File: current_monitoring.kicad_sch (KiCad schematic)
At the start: 24 parts, among them IC3 INA180A1QDBVRQ1, J1 DBG, Q3 PBSS4330X,135, U3 LP5912-3.3DRV, U5 74LS47, U6 ATTINY824-XUR

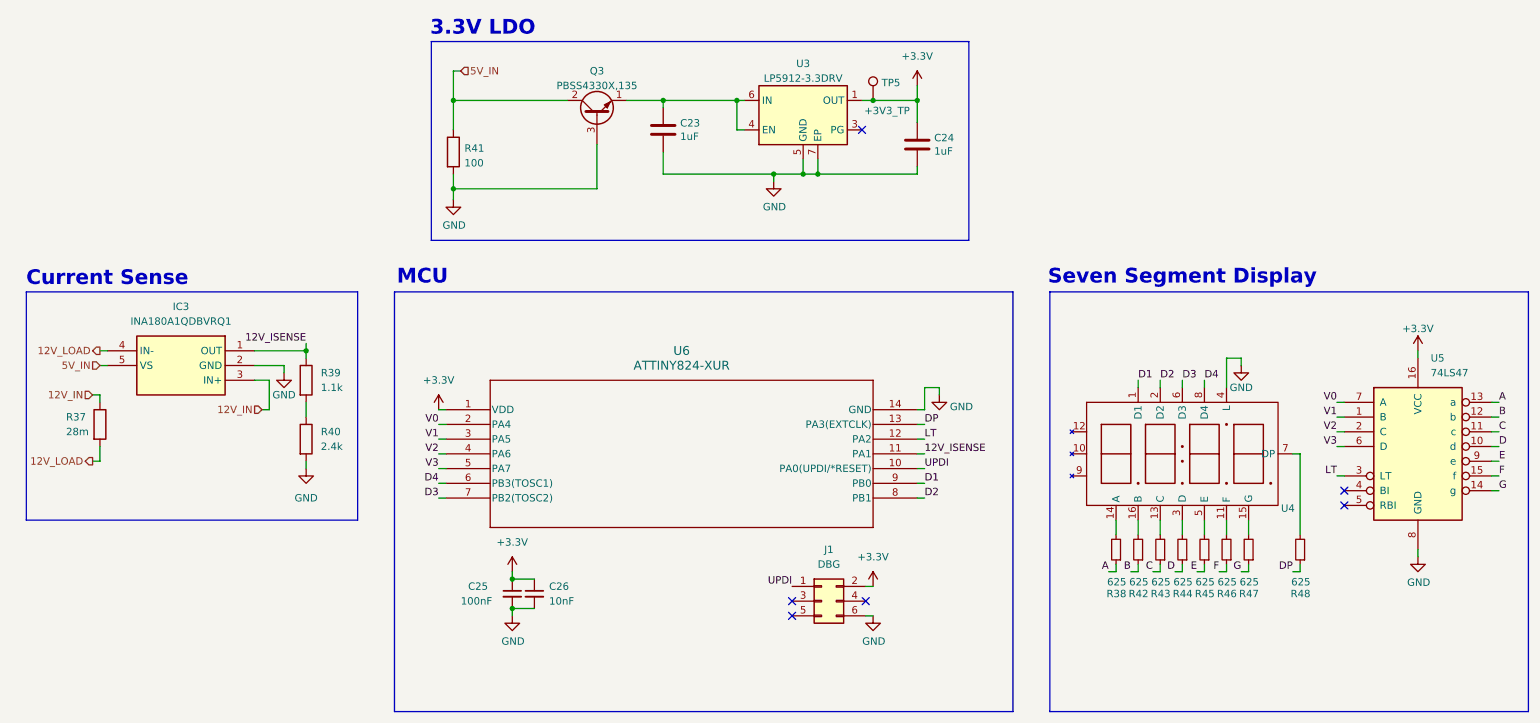
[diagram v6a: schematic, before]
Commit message: updated with some new footprints (have yet to finish footprint assignment; also need to switch out inductor for 5V buck)
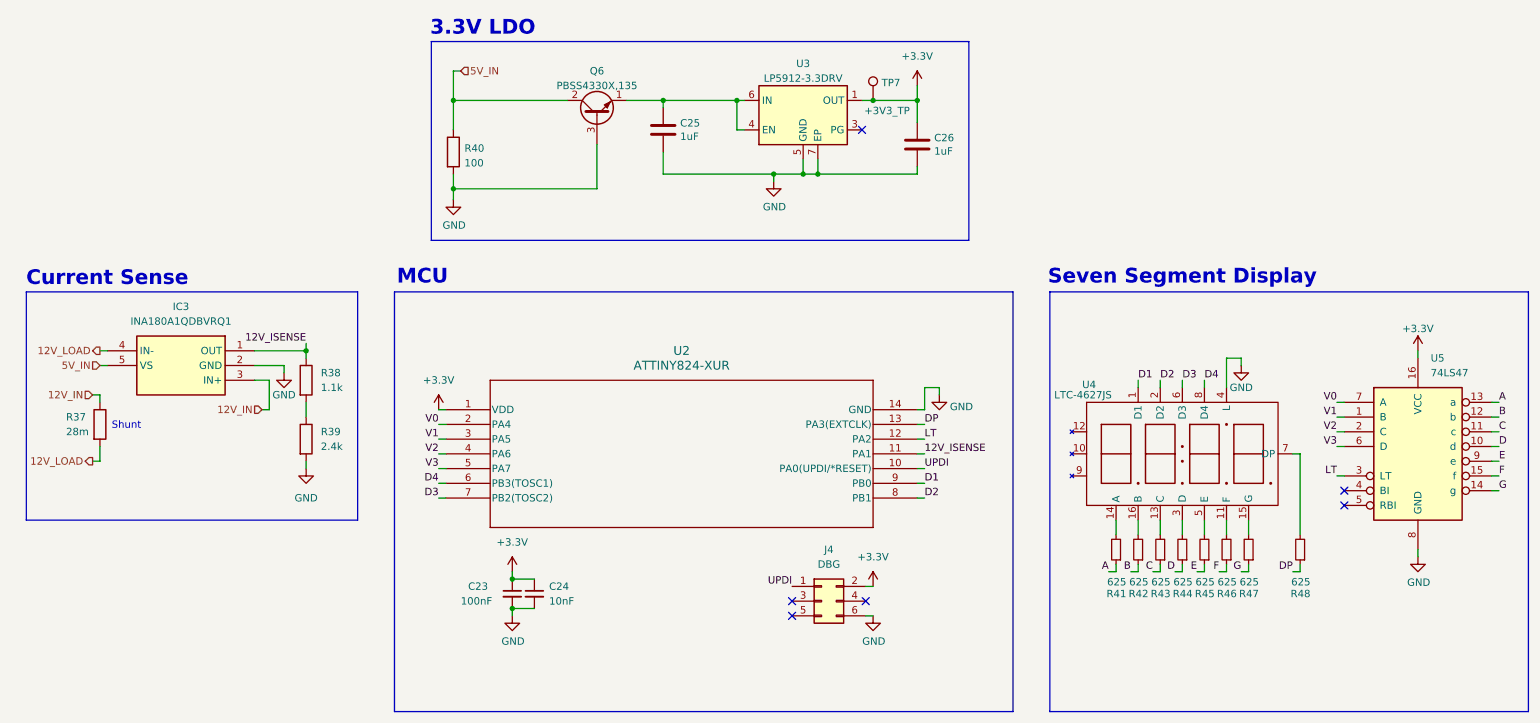
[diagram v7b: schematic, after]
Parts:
- C23: renamed from C25; footprint (none) -> Capacitor_SMD:C_0805_2012Metric
- C24: renamed from C26; footprint (none) -> Capacitor_SMD:C_0805_2012Metric
- IC3: footprint SOT95P280X145-5N -> UTSVT_ICs:SOT95P280X145-5N
- R37: Mouser Part Number (none) -> PE2512FKE7W0R028L
- R38: renamed from R39; footprint (none) -> Resistor_SMD:R_0805_2012Metric
- R39: renamed from R40; footprint (none) -> Resistor_SMD:R_0805_2012Metric
- R41: renamed from R38; footprint (none) -> Resistor_SMD:R_0805_2012Metric
- R42, R43, R44, R45, R46, R47, R48: footprint (none) -> Resistor_SMD:R_0805_2012Metric
- TP7: renamed from TP5; footprint Connector_PinHeader_2.54mm:PinHeader_1x01_P2.54mm_Vertical -> TestPoint:TestPoint_Pad_D2.5mm
- U2: renamed from U6; footprint TSSOP14_ST_MCH -> Package_SO:TSSOP-14-1EP_4.4x5mm_P0.65mm
- U4: value ~ -> LTC-4627JS; footprint (none) -> Package_DIP:DIP-14_W10.16mm_LongPads
- renumbered C23 to C25, C24 to C26, J1 to J4, Q3 to Q6, R41 to R40
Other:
- note added: "Shunt"

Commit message: changed 5v buck to TPS56A37
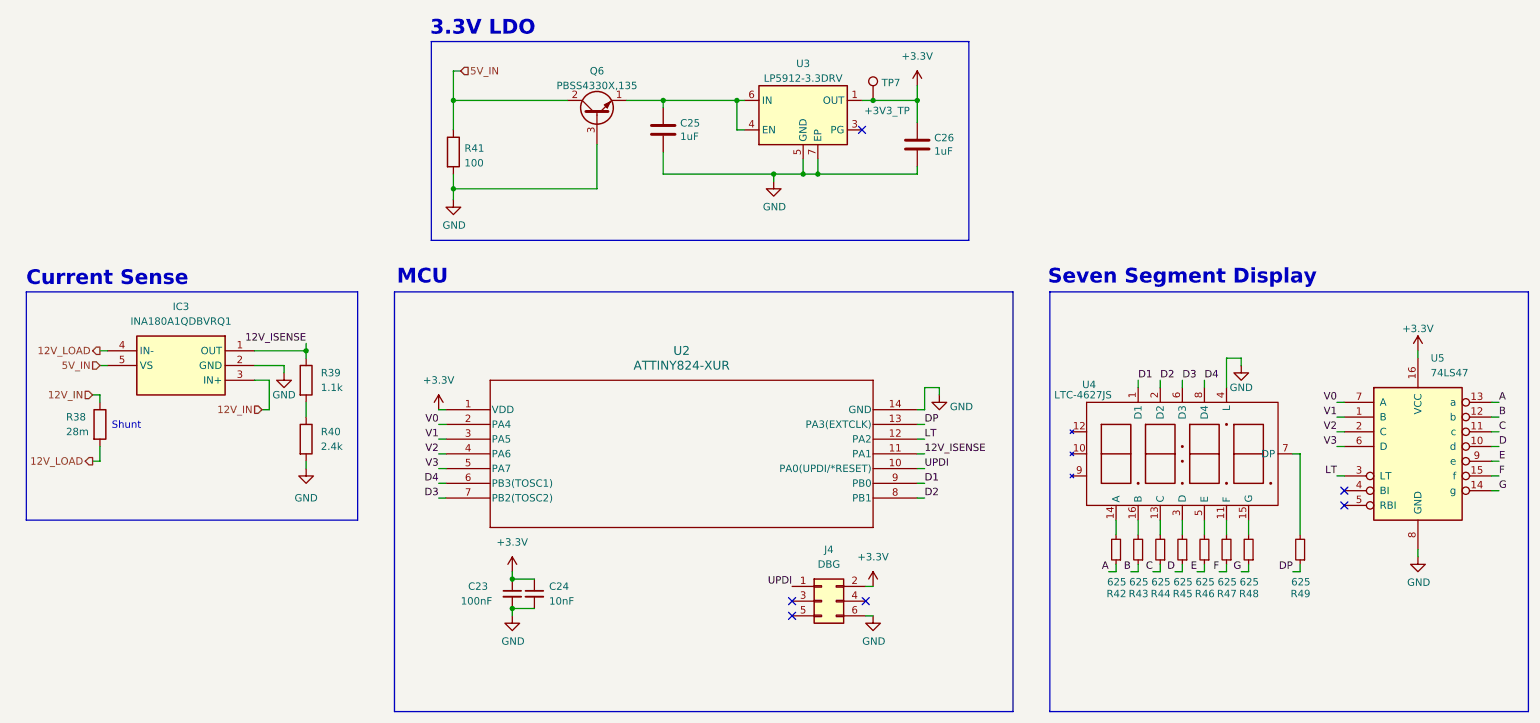
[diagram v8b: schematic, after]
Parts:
- renumbered R37 to R38, R38 to R39, R39 to R40, R40 to R41, R41 to R42, R42 to R43, R43 to R44, R44 to R45, R45 to R46, R46 to R47, R47 to R48, R48 to R49
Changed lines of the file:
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@@
 		(on_board yes)
 		(dnp no)
-		(property "Reference" "R43"
+		(property "Reference" "R44"
 			(at 217.678 121.92 0)
 			(effects
@@
 			(project "USBCPowerPCB"
 				(path "/f58400c5-df4b-4929-8d2b-33c0fe23fcd9/0ba7757f-854f-4573-bb78-e140dbbd3450"
-					(reference "R43")
+					(reference "R44")
 					(unit 1)
 				)
@@
 		(on_board yes)
 		(dnp no)
-		(property "Reference" "R42"
+		(property "Reference" "R43"
 			(at 213.868 121.92 0)
 			(effects
@@
 			(project "USBCPowerPCB"
 				(path "/f58400c5-df4b-4929-8d2b-33c0fe23fcd9/0ba7757f-854f-4573-bb78-e140dbbd3450"
-					(reference "R42")
+					(reference "R43")
 					(unit 1)
 				)
@@
 		(on_board yes)
 		(dnp no)
-		(property "Reference" "R46"
+		(property "Reference" "R47"
 			(at 229.108 121.92 0)
 			(effects
@@
 			(project "USBCPowerPCB"
 				(path "/f58400c5-df4b-4929-8d2b-33c0fe23fcd9/0ba7757f-854f-4573-bb78-e140dbbd3450"
-					(reference "R46")
+					(reference "R47")
 					(unit 1)
 				)
@@
 		(on_board yes)
 		(dnp no)
-		(property "Reference" "R44"
+		(property "Reference" "R45"
 			(at 221.488 121.92 0)
 			(effects
@@
 			(project "USBCPowerPCB"
 				(path "/f58400c5-df4b-4929-8d2b-33c0fe23fcd9/0ba7757f-854f-4573-bb78-e140dbbd3450"
-					(reference "R44")
+					(reference "R45")
 					(unit 1)
 				)
@@
 		(on_board yes)
 		(dnp no)
-		(property "Reference" "#PWR045"
+		(property "Reference" "#PWR047"
 			(at 166.37 132.08 0)
 			(effects
@@
 			(project "USBCPowerPCB"
 				(path "/f58400c5-df4b-4929-8d2b-33c0fe23fcd9/0ba7757f-854f-4573-bb78-e140dbbd3450"
-					(reference "#PWR045")
+					(reference "#PWR047")
 					(unit 1)
 				)
@@
 		(dnp no)
 		(fields_autoplaced yes)
-		(property "Reference" "#PWR039"
+		(property "Reference" "#PWR041"
 			(at 91.44 93.98 0)
 			(effects
@@
 			(project "USBCPowerPCB"
 				(path "/f58400c5-df4b-4929-8d2b-33c0fe23fcd9/0ba7757f-854f-4573-bb78-e140dbbd3450"
-					(reference "#PWR039")
+					(reference "#PWR041")
 					(unit 1)
 				)
@@
 		(on_board yes)
 		(dnp no)
-		(property "Reference" "#PWR037"
+		(property "Reference" "#PWR039"
 			(at 64.77 90.17 0)
 			(effects
@@
 			(project "USBCPowerPCB"
 				(path "/f58400c5-df4b-4929-8d2b-33c0fe23fcd9/0ba7757f-854f-4573-bb78-e140dbbd3450"
-					(reference "#PWR037")
+					(reference "#PWR039")
 					(unit 1)
 				)
@@
 		(on_board yes)
 		(dnp no)
-		(property "Reference" "R48"
+		(property "Reference" "R49"
 			(at 241.808 121.92 0)
 			(effects
@@
 			(project "USBCPowerPCB"
 				(path "/f58400c5-df4b-4929-8d2b-33c0fe23fcd9/0ba7757f-854f-4573-bb78-e140dbbd3450"
-					(reference "R48")
+					(reference "R49")
 					(unit 1)
 				)
@@
 		(dnp no)
 		(fields_autoplaced yes)
-		(property "Reference" "#PWR041"
+		(property "Reference" "#PWR043"
 			(at 104.14 121.92 0)
 			(effects
@@
 			(project "USBCPowerPCB"
 				(path "/f58400c5-df4b-4929-8d2b-33c0fe23fcd9/0ba7757f-854f-4573-bb78-e140dbbd3450"
-					(reference "#PWR041")
+					(reference "#PWR043")
 					(unit 1)
 				)
@@
 		(on_board yes)
 		(dnp no)
-		(property "Reference" "#PWR048"
+		(property "Reference" "#PWR050"
 			(at 229.87 88.9 0)
 			(effects
@@
 			(project ""
 				(path "/f58400c5-df4b-4929-8d2b-33c0fe23fcd9/0ba7757f-854f-4573-bb78-e140dbbd3450"
-					(reference "#PWR048")
+					(reference "#PWR050")
 					(unit 1)
 				)
@@
 		(dnp no)
 		(fields_autoplaced yes)
-		(property "Reference" "R38"
+		(property "Reference" "R39"
 			(at 71.12 83.8199 0)
 			(effects
@@
 			(project "USBCPowerPCB"
 				(path "/f58400c5-df4b-4929-8d2b-33c0fe23fcd9/0ba7757f-854f-4573-bb78-e140dbbd3450"
-					(reference "R38")
+					(reference "R39")
 					(unit 1)
 				)
@@
 		(on_board yes)
 		(dnp no)
-		(property "Reference" "#PWR043"
+		(property "Reference" "#PWR045"
 			(at 149.225 57.15 0)
 			(effects
@@
 			(project "USBCPowerPCB"
 				(path "/f58400c5-df4b-4929-8d2b-33c0fe23fcd9/0ba7757f-854f-4573-bb78-e140dbbd3450"
-					(reference "#PWR043")
+					(reference "#PWR045")
 					(unit 1)
 				)
@@
 		(on_board yes)
 		(dnp no)
-		(property "Reference" "#PWR047"
+		(property "Reference" "#PWR049"
 			(at 177.8 93.98 0)
 			(effects
@@
 			(project "USBCPowerPCB"
 				(path "/f58400c5-df4b-4929-8d2b-33c0fe23fcd9/0ba7757f-854f-4573-bb78-e140dbbd3450"
-					(reference "#PWR047")
+					(reference "#PWR049")
 					(unit 1)
 				)
@@
 		(dnp no)
 		(fields_autoplaced yes)
-		(property "Reference" "#PWR044"
+		(property "Reference" "#PWR046"
 			(at 166.37 124.46 0)
 			(effects
@@
 			(project "USBCPowerPCB"
 				(path "/f58400c5-df4b-4929-8d2b-33c0fe23fcd9/0ba7757f-854f-4573-bb78-e140dbbd3450"
-					(reference "#PWR044")
+					(reference "#PWR046")
 					(unit 1)
 				)
@@
 		(on_board yes)
 		(dnp no)
-		(property "Reference" "R41"
+		(property "Reference" "R42"
 			(at 210.058 121.92 0)
 			(effects
@@
 			(project "USBCPowerPCB"
 				(path "/f58400c5-df4b-4929-8d2b-33c0fe23fcd9/0ba7757f-854f-4573-bb78-e140dbbd3450"
-					(reference "R41")
+					(reference "R42")
 					(unit 1)
 				)
@@
 		(on_board yes)
 		(dnp no)
-		(property "Reference" "R37"
+		(property "Reference" "R38"
 			(at 27.178 91.44 0)
 			(effects
@@
 			(project "USBCPowerPCB"
 				(path "/f58400c5-df4b-4929-8d2b-33c0fe23fcd9/0ba7757f-854f-4573-bb78-e140dbbd3450"
-					(reference "R37")
+					(reference "R38")
 					(unit 1)
 				)
@@
 		(on_board yes)
 		(dnp no)
-		(property "Reference" "R45"
+		(property "Reference" "R46"
 			(at 225.298 121.92 0)
 			(effects
@@
 			(project "USBCPowerPCB"
 				(path "/f58400c5-df4b-4929-8d2b-33c0fe23fcd9/0ba7757f-854f-4573-bb78-e140dbbd3450"
-					(reference "R45")
+					(reference "R46")
 					(unit 1)
 				)
@@
 		(dnp no)
 		(fields_autoplaced yes)
-		(property "Reference" "R39"
+		(property "Reference" "R40"
 			(at 71.12 93.9799 0)
 			(effects
@@
 			(project "USBCPowerPCB"
 				(path "/f58400c5-df4b-4929-8d2b-33c0fe23fcd9/0ba7757f-854f-4573-bb78-e140dbbd3450"
-					(reference "R39")
+					(reference "R40")
 					(unit 1)
 				)
@@
 		(on_board yes)
 		(dnp no)
-		(property "Reference" "R47"
+		(property "Reference" "R48"
 			(at 232.918 121.92 0)
 			(effects
@@
 			(project "USBCPowerPCB"
 				(path "/f58400c5-df4b-4929-8d2b-33c0fe23fcd9/0ba7757f-854f-4573-bb78-e140dbbd3450"
-					(reference "R47")
+					(reference "R48")
 					(unit 1)
 				)
@@
 		(on_board yes)
 		(dnp no)
-		(property "Reference" "#PWR040"
+		(property "Reference" "#PWR042"
 			(at 93.98 60.325 0)
 			(effects
@@
 			(project "USBCPowerPCB"
 				(path "/f58400c5-df4b-4929-8d2b-33c0fe23fcd9/0ba7757f-854f-4573-bb78-e140dbbd3450"
-					(reference "#PWR040")
+					(reference "#PWR042")
 					(unit 1)
 				)
@@
 		(dnp no)
 		(fields_autoplaced yes)
-		(property "Reference" "R40"
+		(property "Reference" "R41"
 			(at 95.885 45.085 0)
 			(effects
@@
 			(project "USBCPowerPCB"
 				(path "/f58400c5-df4b-4929-8d2b-33c0fe23fcd9/0ba7757f-854f-4573-bb78-e140dbbd3450"
-					(reference "R40")
+					(reference "R41")
 					(unit 1)
 				)
@@
 		(on_board yes)
 		(dnp no)
-		(property "Reference" "#PWR049"
+		(property "Reference" "#PWR051"
 			(at 260.35 83.82 0)
 			(effects
@@
 			(project "USBCPowerPCB"
 				(path "/f58400c5-df4b-4929-8d2b-33c0fe23fcd9/0ba7757f-854f-4573-bb78-e140dbbd3450"
-					(reference "#PWR049")
+					(reference "#PWR051")
 					(unit 1)
 				)
@@
 		(on_board yes)
 		(dnp no)
-		(property "Reference" "#PWR042"
+		(property "Reference" "#PWR044"
 			(at 104.14 132.08 0)
 			(effects
@@
 			(project "USBCPowerPCB"
 				(path "/f58400c5-df4b-4929-8d2b-33c0fe23fcd9/0ba7757f-854f-4573-bb78-e140dbbd3450"
-					(reference "#PWR042")
+					(reference "#PWR044")
 					(unit 1)
 				)
@@
 		(dnp no)
 		(fields_autoplaced yes)
-		(property "Reference" "#PWR038"
+		(property "Reference" "#PWR040"
 			(at 68.58 106.68 0)
 			(effects
@@
 			(project "USBCPowerPCB"
 				(path "/f58400c5-df4b-4929-8d2b-33c0fe23fcd9/0ba7757f-854f-4573-bb78-e140dbbd3450"
-					(reference "#PWR038")
+					(reference "#PWR040")
 					(unit 1)
 				)
@@
 		(on_board yes)
 		(dnp no)
-		(property "Reference" "#PWR050"
+		(property "Reference" "#PWR052"
 			(at 260.35 121.92 0)
 			(effects
@@
 			(project "USBCPowerPCB"
 				(path "/f58400c5-df4b-4929-8d2b-33c0fe23fcd9/0ba7757f-854f-4573-bb78-e140dbbd3450"
-					(reference "#PWR050")
+					(reference "#PWR052")
 					(unit 1)
 				)
@@
 		(dnp no)
 		(fields_autoplaced yes)
-		(property "Reference" "#PWR046"
+		(property "Reference" "#PWR048"
 			(at 173.99 38.1 0)
 			(effects
@@
 			(project ""
 				(path "/f58400c5-df4b-4929-8d2b-33c0fe23fcd9/0ba7757f-854f-4573-bb78-e140dbbd3450"
-					(reference "#PWR046")
-					(unit 1)
-				)
+					(reference "#PWR048")
+					(unit 1)
+				)
